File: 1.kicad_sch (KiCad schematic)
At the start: 24 parts, among them J1 Screw_Terminal_01x03, J2 Screw_Terminal_01x01, J3 Screw_Terminal_01x01, U1 LTC2990, U2 LTC2990, U3 LTC2990

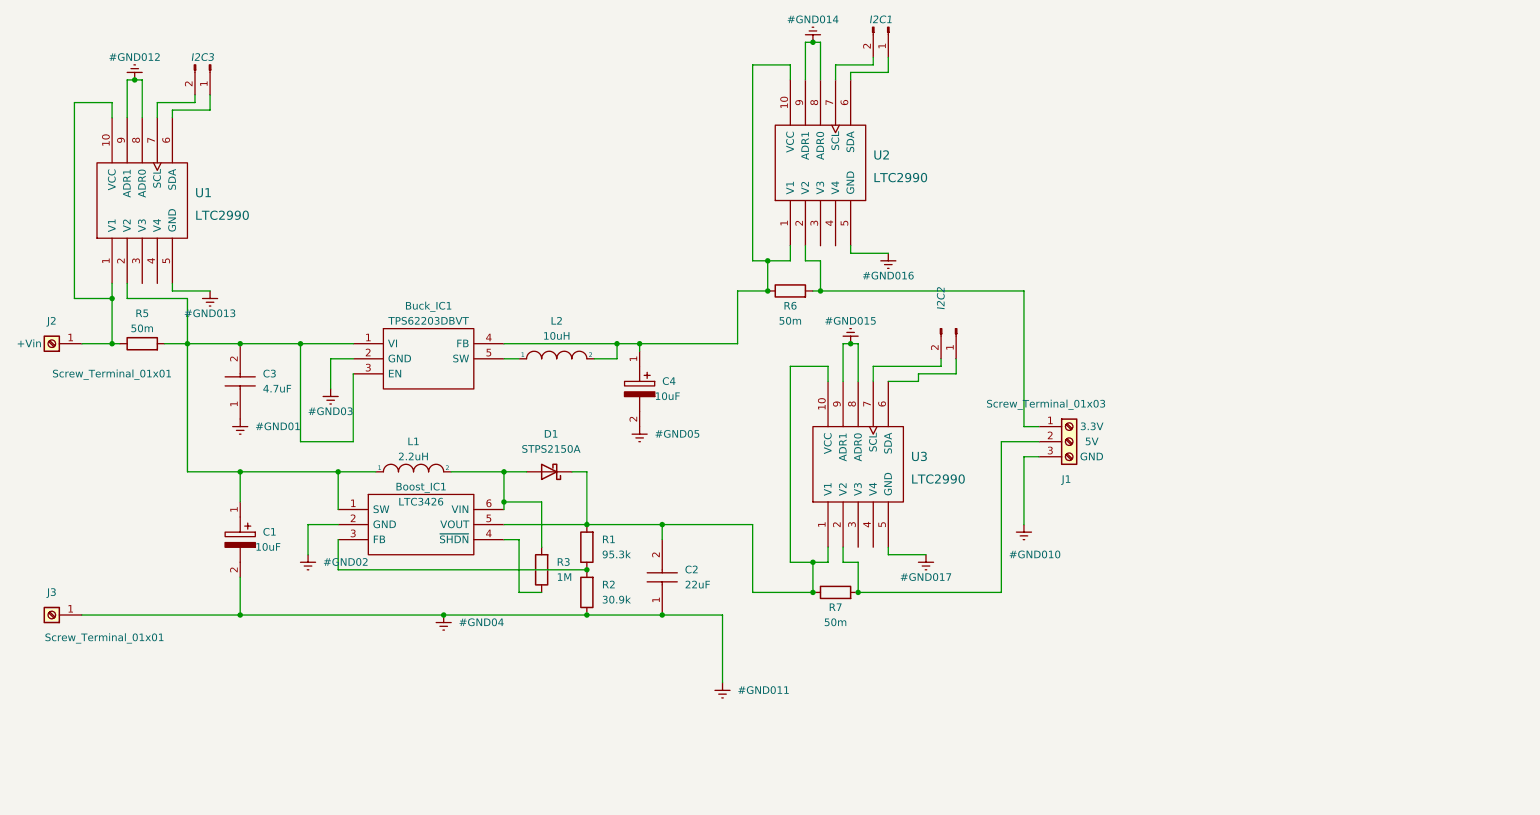
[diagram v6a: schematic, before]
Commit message: Start redesign coz boost circuit is f'd up
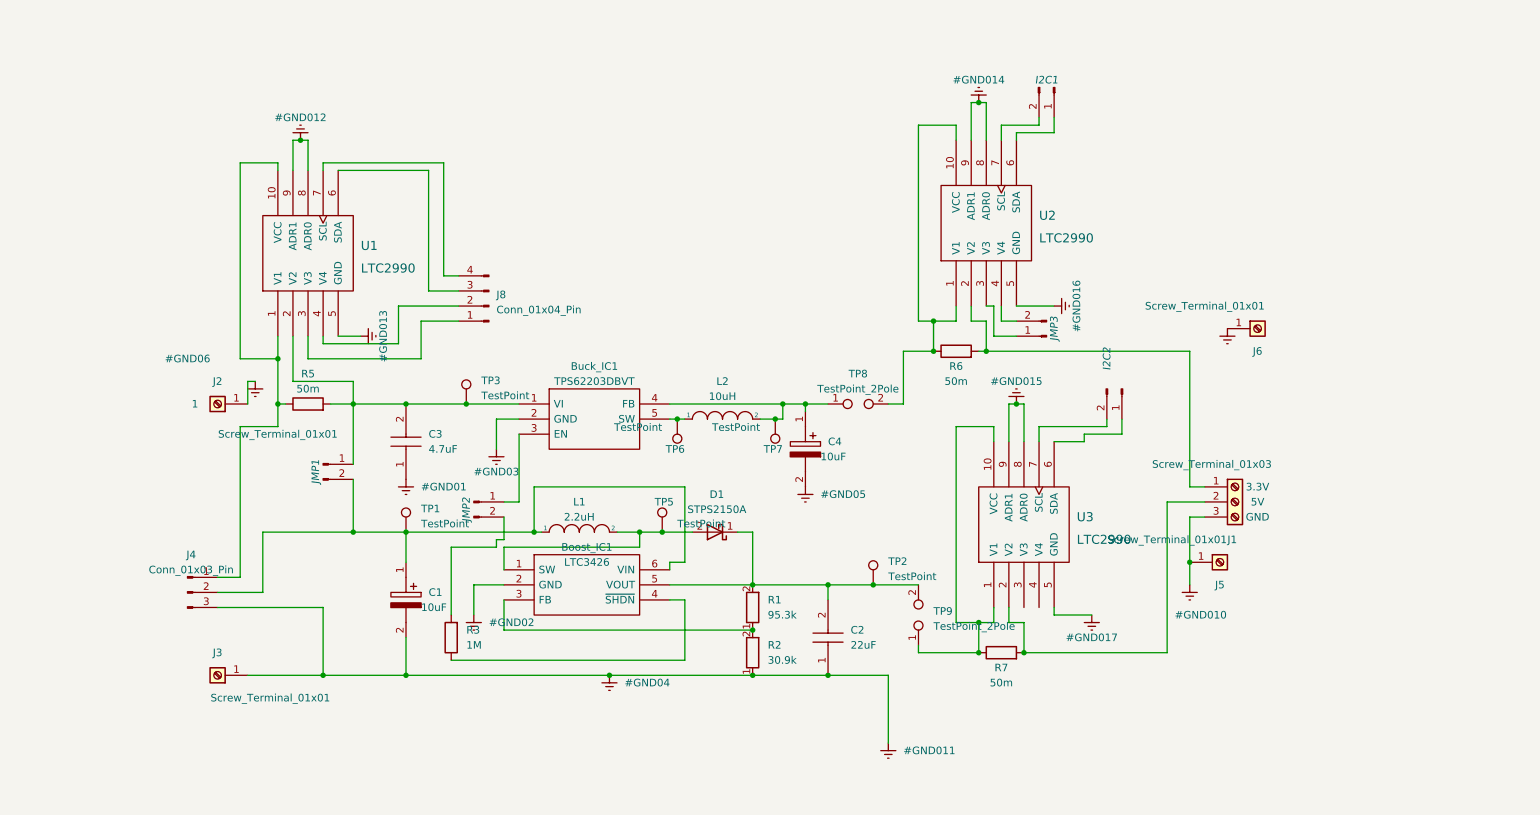
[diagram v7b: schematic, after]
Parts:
- removed I2C3: EN, Connector_PinHeader_1.00mm:PinHeader_1x02_P1.00mm_Vertical, symbol Connector:Conn_01x02_Male
- added J4: Conn_01x03_Pin, TerminalBlock_Phoenix:TerminalBlock_Phoenix_MKDS-1,5-3_1x03_P5.00mm_Horizontal, symbol Connector:Conn_01x03_Pin
- added J5, J6: Screw_Terminal_01x01, Connector_Pin:Pin_D1.3mm_L11.0mm_LooseFit, symbol Connector:Screw_Terminal_01x01
- added J8: Conn_01x04_Pin, Connector_PinHeader_2.54mm:PinHeader_1x04_P2.54mm_Vertical, symbol Connector:Conn_01x04_Pin
- added JMP1, JMP2, JMP3: EN, Connector_PinHeader_2.54mm:PinHeader_1x02_P2.54mm_Vertical, symbol Connector:Conn_01x02_Male
- added TP1, TP2, TP3, TP5, TP6, TP7: TestPoint, TestPoint:TestPoint_THTPad_1.5x1.5mm_Drill0.7mm, symbol Connector:TestPoint
- added TP8, TP9: TestPoint_2Pole, TestPoint:TestPoint_2Pads_Pitch2.54mm_Drill0.8mm, symbol Connector:TestPoint_2Pole
- I2C1, I2C2: footprint Connector_PinHeader_1.00mm:PinHeader_1x02_P1.00mm_Vertical -> Connector_PinHeader_2.54mm:PinHeader_1x02_P2.54mm_Vertical
- J1: footprint TerminalBlock_MetzConnect:TerminalBlock_MetzConnect_Type055_RT01503HDWU_1x03_P5.00mm_Horizontal -> TerminalBlock_Phoenix:TerminalBlock_Phoenix_MKDS-1,5-3_1x03_P5.00mm_Horizontal
- J2: Field4 +Vin -> 1
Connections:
- net Earth: now also J2.1 (Pin_1), J4.3 (Pin_3), J5.1 (Pin_1), J6.1 (Pin_1)
- net at R5.1, U1.1 (V1), U1.10 (VCC): now also J4.1 (Pin_1); no longer J2.1 (Pin_1)
- net at Buck_IC1.1 (VI), C3.2, R5.2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: now also JMP1.1 (Pin_1), TP3.1; no longer Boost_IC1.1 (SW), Buck_IC1.3 (EN), C1.1, L1.1
- net at U1.3 (V3): now also J8.1 (Pin_1)
- net at U1.4 (V4): now also J8.2 (Pin_2)
- net at U1.6 (SDA): now also J8.3 (Pin_3)
- net at U1.7 (SCL): now also J8.4 (Pin_4)
- net at R6.1, U2.1 (V1), U2.10 (VCC): now also TP8.2; no longer Buck_IC1.4 (FB), C4.1, L2.2
- net at U2.3 (V3): now also JMP3.1 (Pin_1)
- net at U2.4 (V4): now also JMP3.2 (Pin_2)
- net at Boost_IC1.5 (VOUT), C2.2, D1.1 (K)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: now also TP2.1, TP9.2; no longer R7.1, U3.1 (V1), U3.10 (VCC)
- net at D1.2 (A), L1.2: now also Boost_IC1.1 (SW), TP5.1; no longer Boost_IC1.6 (VIN), R3.2
- net at Buck_IC1.5 (SW), L2.1: now also TP6.1
- new net: Boost_IC1.6 (VIN), C1.1, J4.2 (Pin_2), JMP1.2 (Pin_2), L1.1, TP1.1
- new net: Buck_IC1.4 (FB), C4.1, L2.2, TP7.1, TP8.1
- new net: R7.1, TP9.1, U3.1 (V1), U3.10 (VCC)
- new net: Buck_IC1.3 (EN), JMP2.1 (Pin_1)
- new net: JMP2.2 (Pin_2), R3.2
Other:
- moved on the sheet: Boost_IC1, Buck_IC1, C1, C2, C3, C4, I2C1, I2C2, J1, J2, J3, L1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

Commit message: Almost there
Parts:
- removed I2C1, I2C2, JMP2, JMP3: EN, Connector_PinHeader_2.54mm:PinHeader_1x02_P2.54mm_Vertical, symbol Connector:Conn_01x02_Male
- removed R6, R7: 50m, 50m RST:RESC3216X88N, symbol Device:R
- removed TP2, TP7: TestPoint, TestPoint:TestPoint_THTPad_1.5x1.5mm_Drill0.7mm, symbol Connector:TestPoint
- removed U2, U3: LTC2990, MON & PROTECC:SOP50P490X110-10N, symbol curr volt mon:LTC2990
- added J7, J9: Conn_01x01_Pin, Connector_PinHeader_2.54mm:PinHeader_1x01_P2.54mm_Vertical, symbol Connector:Conn_01x01_Pin
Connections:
- net at TP8.2: now also J1.1 (Pin_1)
- net at J1.2 (Pin_2): now also TP9.1
- net at Buck_IC1.3 (EN): now also J7.1 (Pin_1)
- net at R3.2: now also J9.1 (Pin_1)
